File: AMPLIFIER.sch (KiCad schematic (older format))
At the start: 46 parts, among them U403 DRV8601, U405 TS5A22366, U406 MP34DT01TR, U407 MP34DT01TR

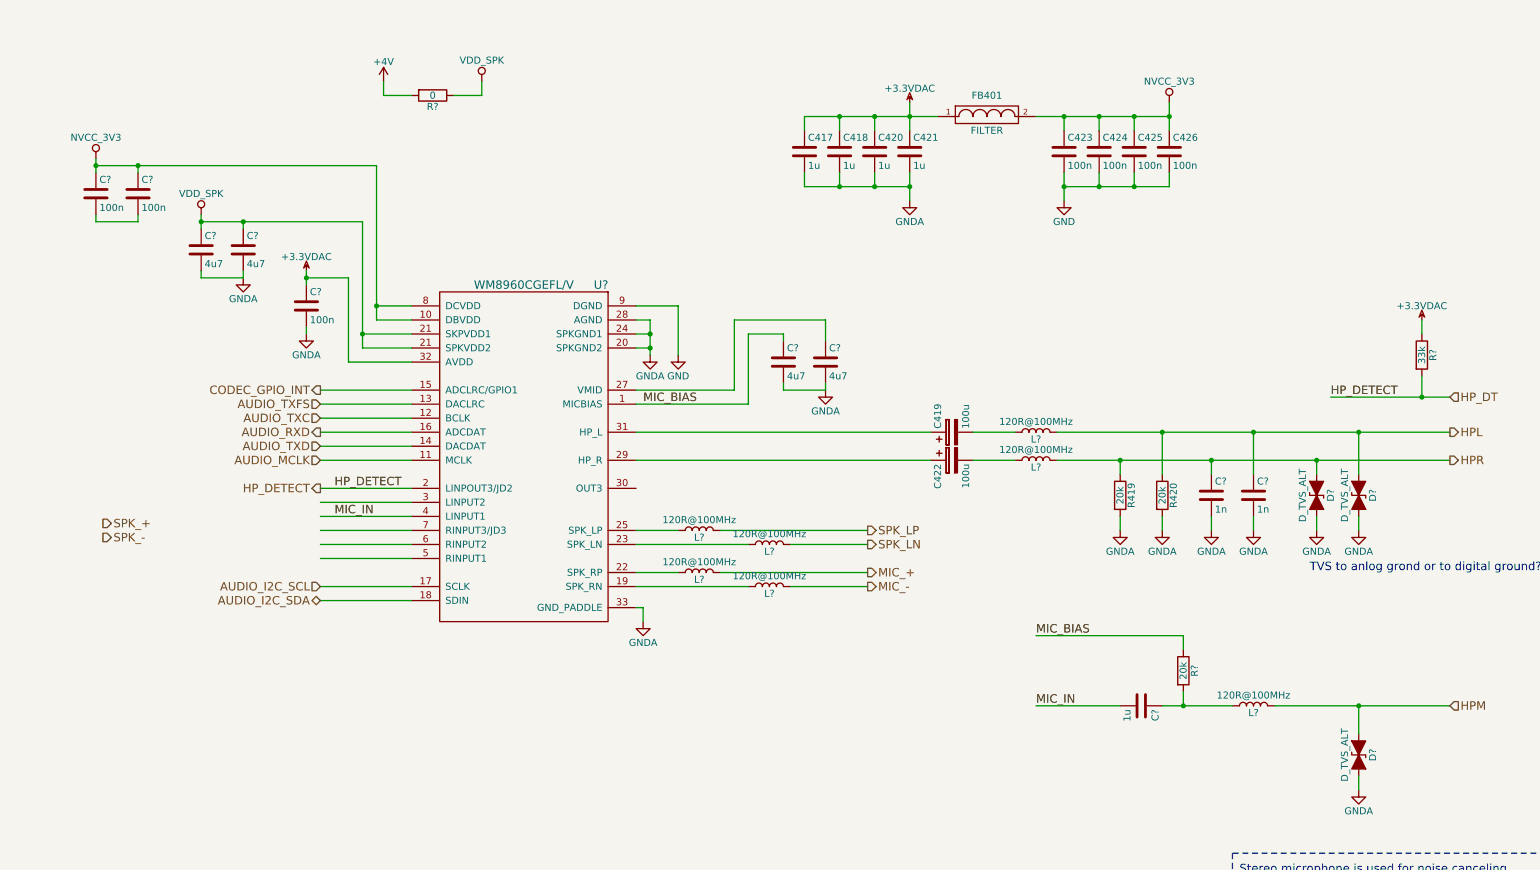
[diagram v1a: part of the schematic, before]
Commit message: Prepare for two battery types NiMH battery for using the original battery pack LiPo battery for using long lasting modern battery
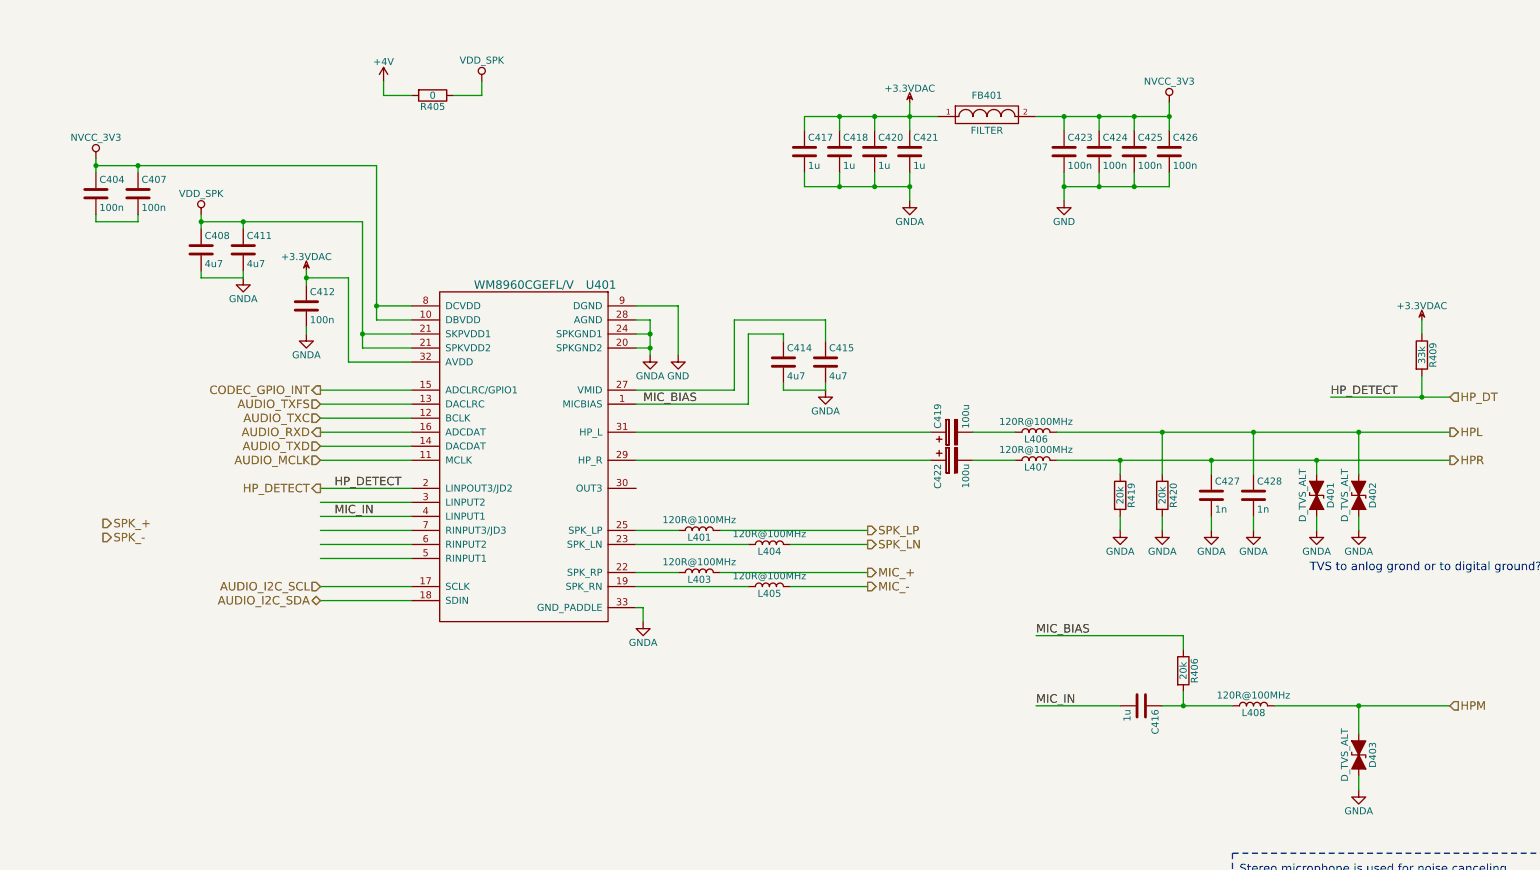
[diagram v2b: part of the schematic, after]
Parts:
- gave numbers to parts that had none: 24

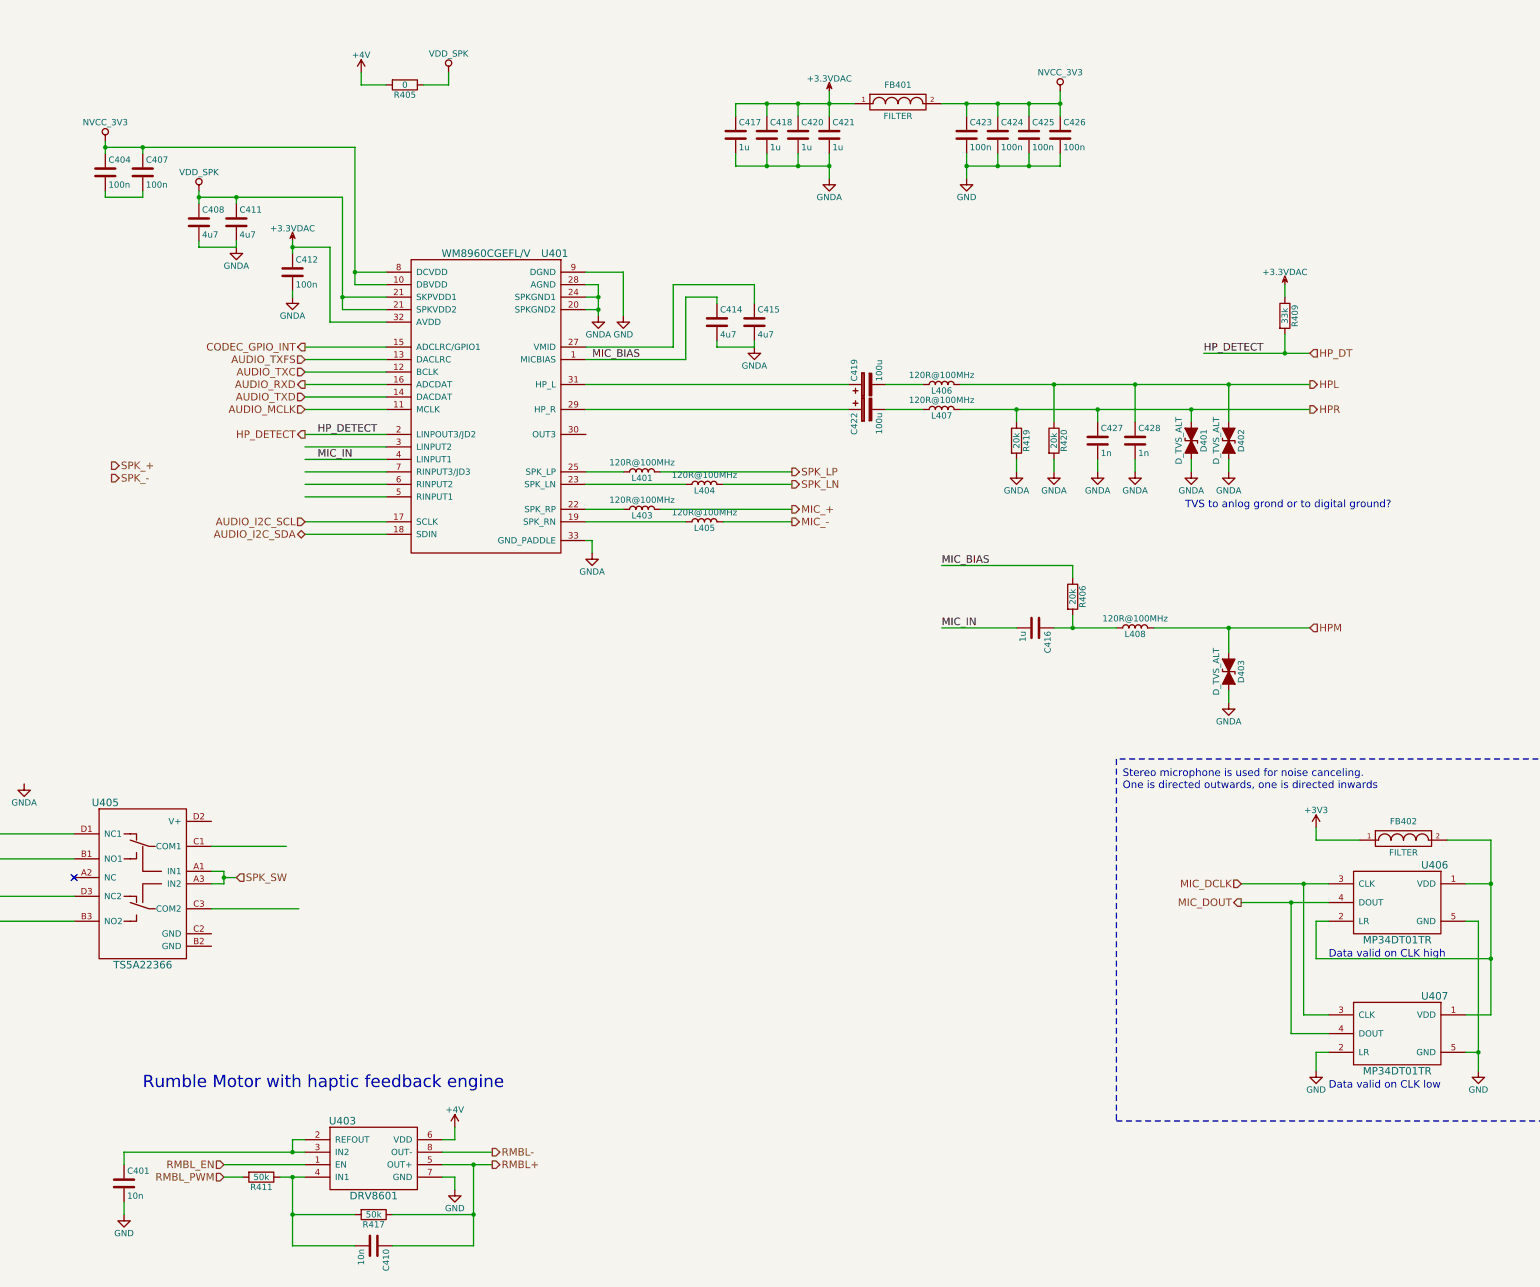
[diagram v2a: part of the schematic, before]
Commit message: Changed several voltage rail connections Removed non existing rails Added circuit for NiMH charging
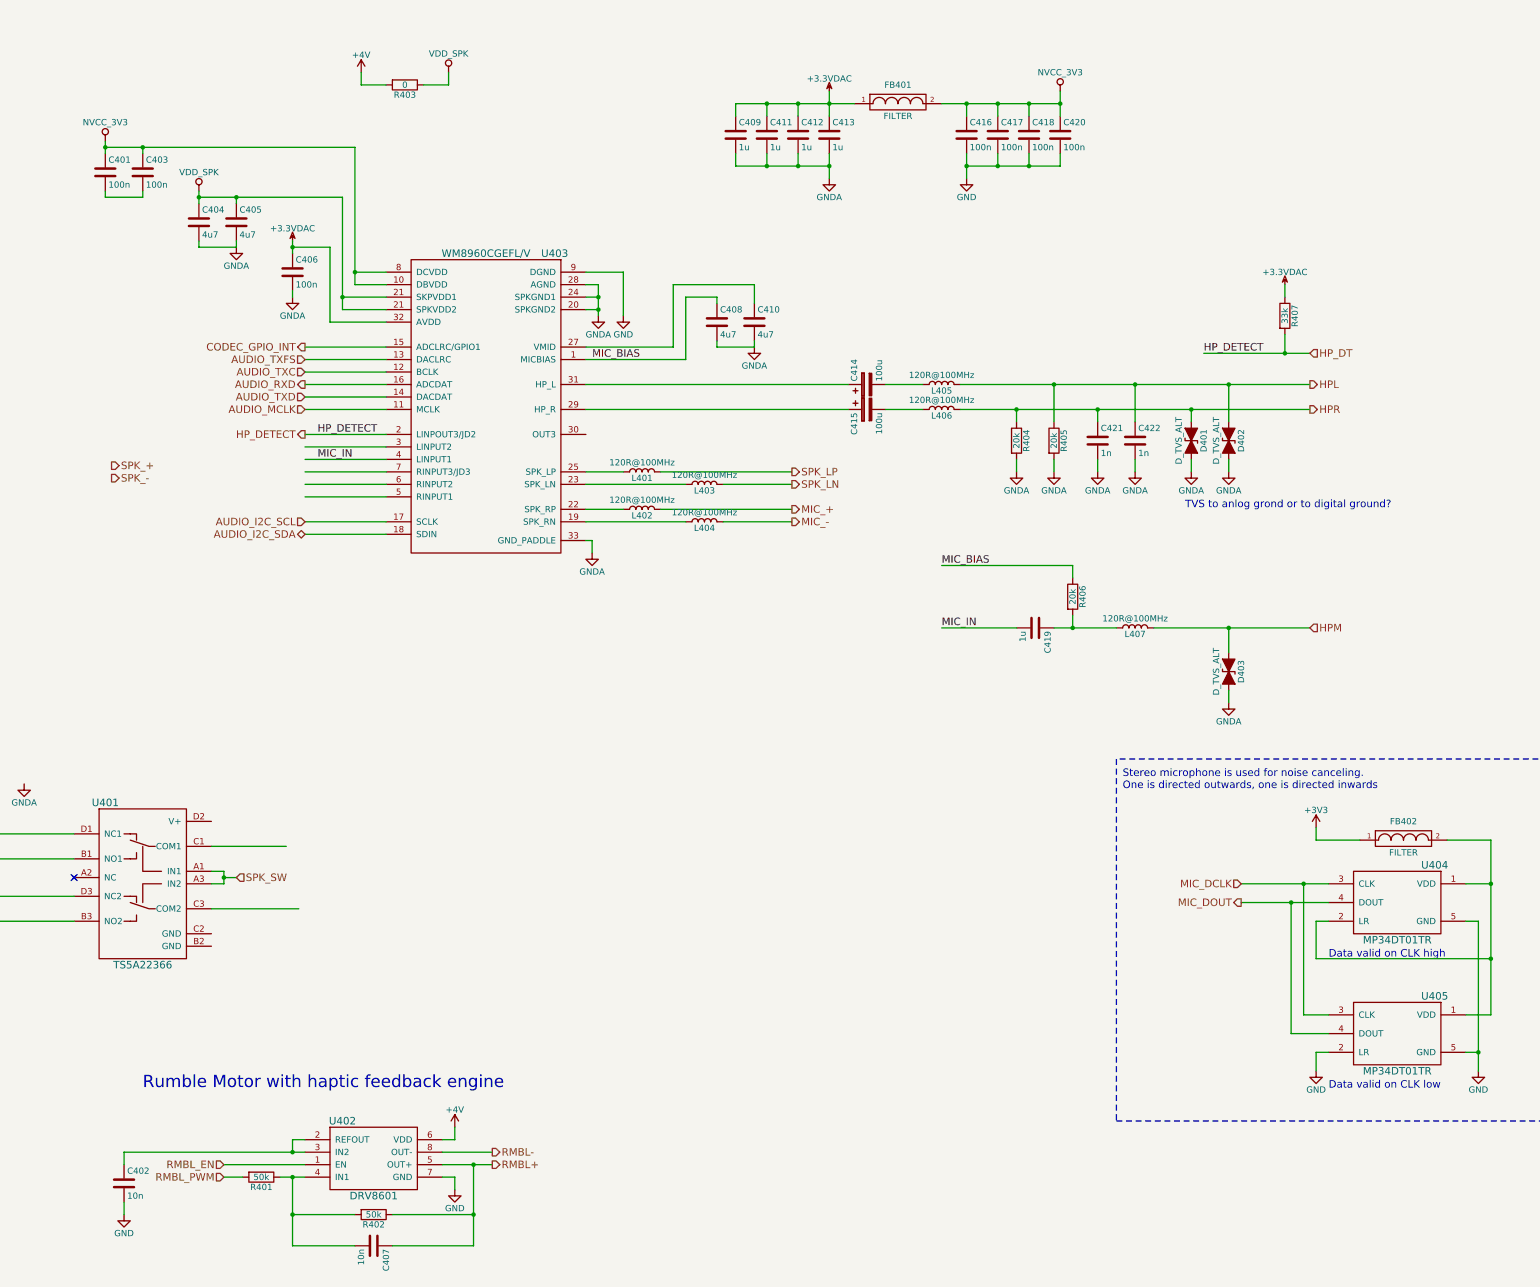
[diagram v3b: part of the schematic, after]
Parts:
- renumbered C404 to C401, C401 to C402, C407 to C403, C408 to C404, C411 to C405, C412 to C406, C410 to C407, C414 to C408, C417 to C409, C415 to C410, C418 to C411, C420 to C412, C421 to C413, C419 to C414, C422 to C415, C423 to C416, C424 to C417, C425 to C418, C416 to C419, C426 to C420, C427 to C421, C428 to C422, L403 to L402, L404 to L403, L405 to L404, L406 to L405, L407 to L406, L408 to L407, R411 to R401, R417 to R402, R405 to R403, R419 to R404, R420 to R405, R409 to R407, U405 to U401, U403 to U402, U401 to U403, U406 to U404, U407 to U405
